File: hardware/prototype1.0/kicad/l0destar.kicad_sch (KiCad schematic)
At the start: 14 parts, among them J1 Main connector, J2 Conn_01x20_Socket, J3 Conn_01x20_Socket_21-40, J4 EXT_GPS, J5 INT_GPS, J6 EXT_LTE, J7 INT_LTE

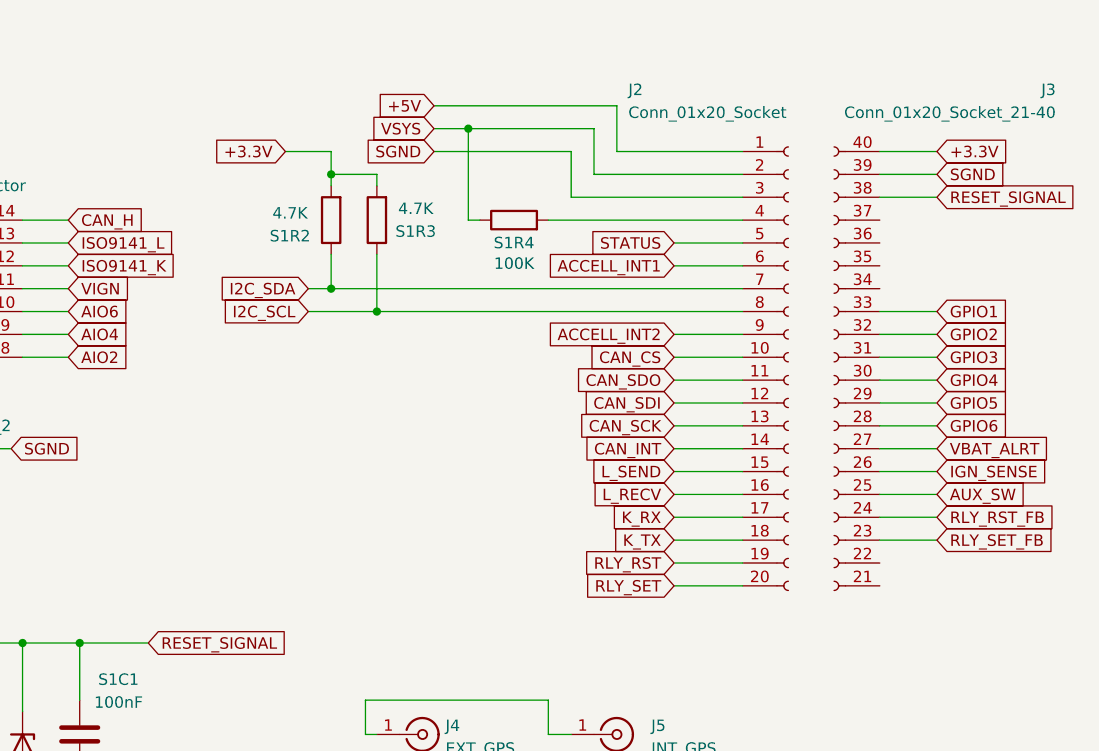
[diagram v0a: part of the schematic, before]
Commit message: updated the ignition sensing voltage divider and added a 4.2 buck to power the ConnectKit board
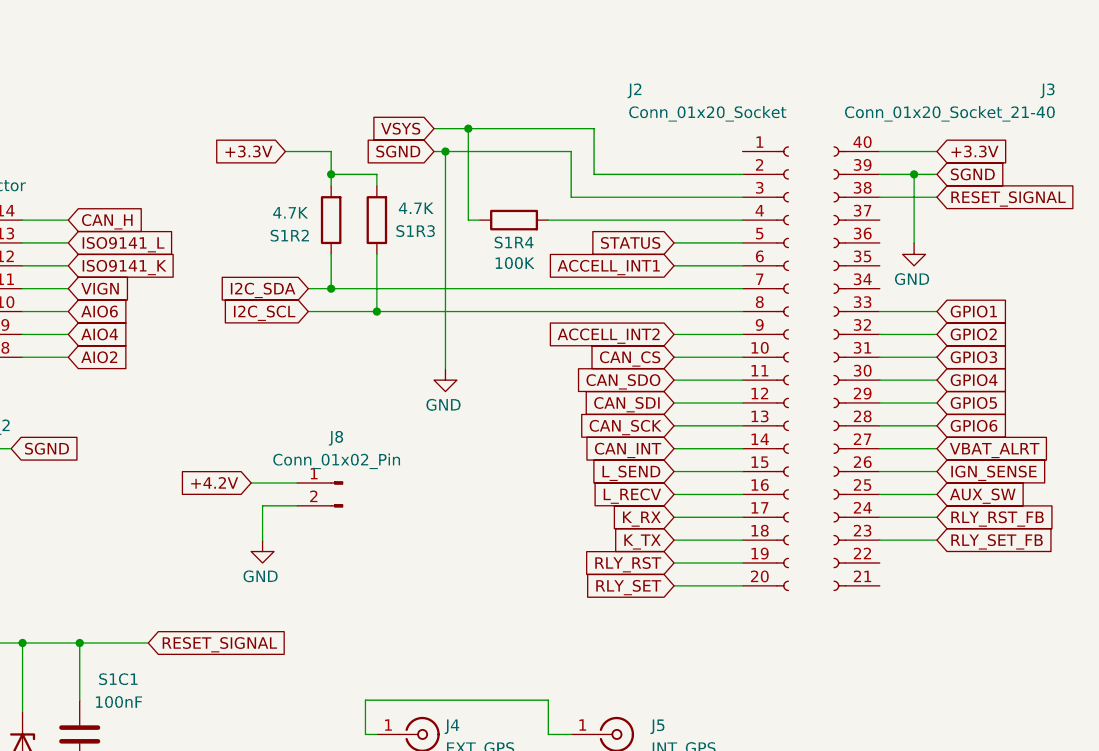
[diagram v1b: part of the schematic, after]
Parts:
- added J8: Conn_01x02_Pin, Connector_PinHeader_2.54mm:PinHeader_1x02_P2.54mm_Vertical, symbol Connector:Conn_01x02_Pin
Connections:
- net SGND is gone; now on net GND: J2.3 (GND), J3.39 (Pin_2), NT1.2
- net GND: now also J8.2 (Pin_2)
- net +5V: no longer names the net of J2.1 (VBUS)
- new net +4.2V: J8.1 (Pin_1)

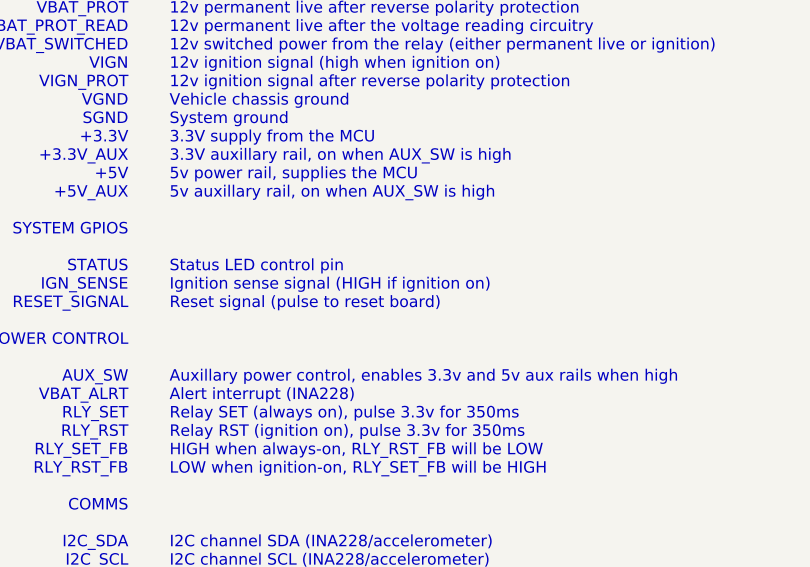
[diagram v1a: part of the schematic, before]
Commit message: replaced the voltage divider that derives the ignition signal with a MOSFET gating the 3.3v rail
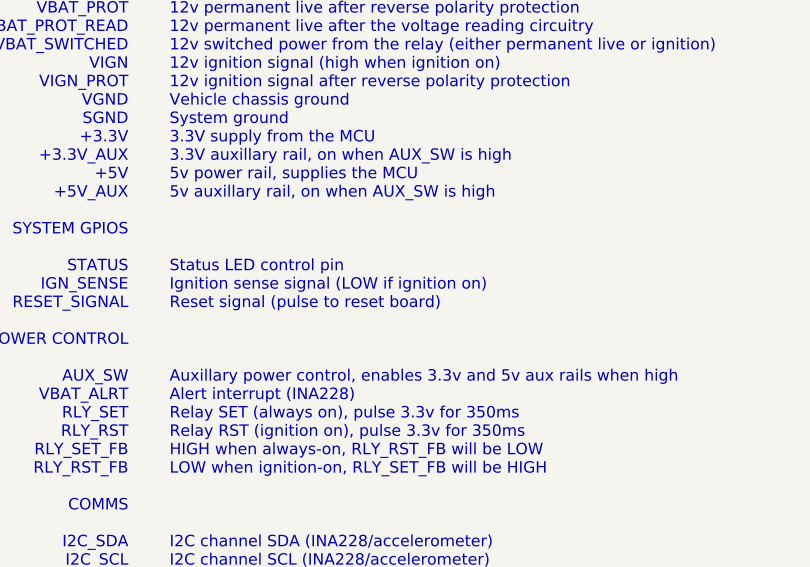
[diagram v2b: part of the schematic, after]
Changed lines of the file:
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@@
 		)
 	)
-	(text "DESCRIPTION\n\n12v permanent live from vehicle\n12v permanent live after reverse polarity protection\n12v permanent live after the voltage reading circuitry\n12v switched power from the relay (either permanent live or ignition)\n12v ignition signal (high when ignition on)\n12v ignition signal after reverse polarity protection\nVehicle chassis ground\nSystem ground\n3.3V supply from the MCU\n3.3V auxillary rail, on when AUX_SW is high\n5v power rail, supplies the MCU\n5v auxillary rail, on when AUX_SW is high\n\n\n\nStatus LED control pin\nIgnition sense signal (HIGH if ignition on)\nReset signal (pulse to reset board)\n\n\n\nAuxillary power control, enables 3.3v and 5v aux rails when high\nAlert interrupt (INA228)\nRelay SET (always on), pulse 3.3v for 350ms\nRelay RST (ignition on), pulse 3.3v for 350ms\nHIGH when always-on, RLY_RST_FB will be LOW\nLOW when ignition-on, RLY_SET_FB will be HIGH\n\n\n\nI2C channel SDA (INA228/accelerometer)\nI2C channel SCL (INA228/accelerometer)\nAccellerometer interrupt 1\nAccellerometer interrupt 2\nCAN CS pin\nCAN SDO pin\nCAN SDI pin\nCAN SCK pin\nCAN INT pin\nK-line RX pin (ISO-9141)\nK-line TX pin (ISO-9141)\nL-line send pin (ISO-9141)\nL-line recv pin (ISO-9141)\nGeneral-purpose GPIO 0-36V\nGeneral-purpose GPIO 0-36V\nGeneral-purpose GPIO 0-36V\nGeneral-purpose GPIO 0-36V\nGeneral-purpose GPIO 0-36V\nGeneral-purpose GPIO 0-36V"
+	(text "DESCRIPTION\n\n12v permanent live from vehicle\n12v permanent live after reverse polarity protection\n12v permanent live after the voltage reading circuitry\n12v switched power from the relay (either permanent live or ignition)\n12v ignition signal (high when ignition on)\n12v ignition signal after reverse polarity protection\nVehicle chassis ground\nSystem ground\n3.3V supply from the MCU\n3.3V auxillary rail, on when AUX_SW is high\n5v power rail, supplies the MCU\n5v auxillary rail, on when AUX_SW is high\n\n\n\nStatus LED control pin\nIgnition sense signal (LOW if ignition on)\nReset signal (pulse to reset board)\n\n\n\nAuxillary power control, enables 3.3v and 5v aux rails when high\nAlert interrupt (INA228)\nRelay SET (always on), pulse 3.3v for 350ms\nRelay RST (ignition on), pulse 3.3v for 350ms\nHIGH when always-on, RLY_RST_FB will be LOW\nLOW when ignition-on, RLY_SET_FB will be HIGH\n\n\n\nI2C channel SDA (INA228/accelerometer)\nI2C channel SCL (INA228/accelerometer)\nAccellerometer interrupt 1\nAccellerometer interrupt 2\nCAN CS pin\nCAN SDO pin\nCAN SDI pin\nCAN SCK pin\nCAN INT pin\nK-line RX pin (ISO-9141)\nK-line TX pin (ISO-9141)\nL-line send pin (ISO-9141)\nL-line recv pin (ISO-9141)\nGeneral-purpose GPIO 0-36V\nGeneral-purpose GPIO 0-36V\nGeneral-purpose GPIO 0-36V\nGeneral-purpose GPIO 0-36V\nGeneral-purpose GPIO 0-36V\nGeneral-purpose GPIO 0-36V"
 		(exclude_from_sim no)
 		(at 201.676 68.326 0)
